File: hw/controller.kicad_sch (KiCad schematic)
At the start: 18 parts, among them J201 43650-0227, U201 NUCLEO-L432KC

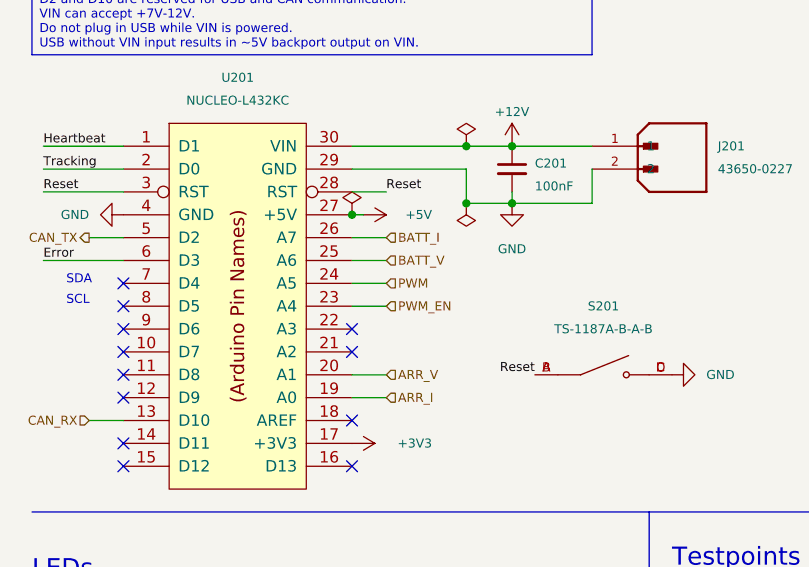
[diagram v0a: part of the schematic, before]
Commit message: bugfix for wrong adc pin for batt current measurements
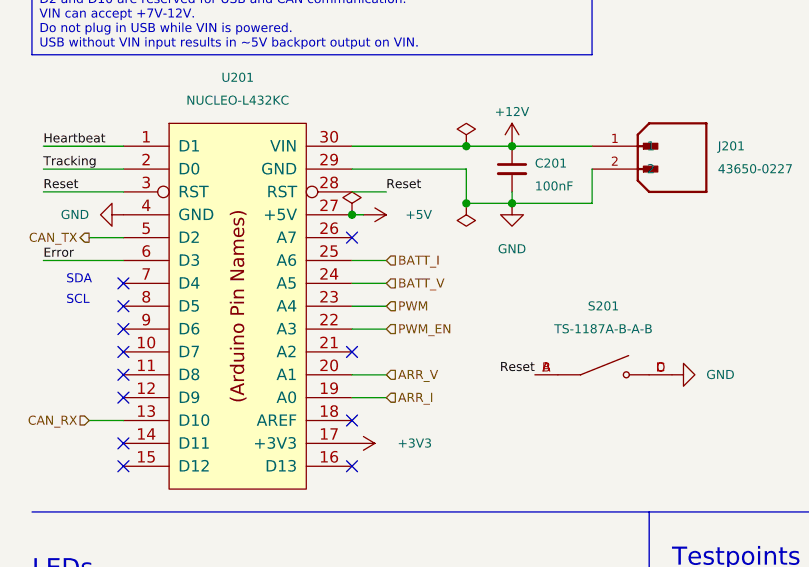
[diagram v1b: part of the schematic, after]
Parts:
- C201: Cost 0.0068 -> 0.0063; LCSC Part # C307331 -> CL05B104KB54PNC; Notes (none) -> Rated for 50V.
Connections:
- net BATT_I: now also U201.25 (A6); no longer U201.26 (A7)
- net BATT_V: now also U201.24 (A5); no longer U201.25 (A6)
- net PWM: now also U201.23 (A4); no longer U201.24 (A5)
- net PWM_EN: now also U201.22 (A3); no longer U201.23 (A4)
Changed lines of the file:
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@@
   (no_connect (at 170.18 82.55))
   (no_connect (at 144.78 74.93))
-  (no_connect (at 170.18 72.39))
   (no_connect (at 144.78 80.01))
   (no_connect (at 144.78 67.31))
   (no_connect (at 170.18 87.63))
   (no_connect (at 144.78 77.47))
+  (no_connect (at 170.18 62.23))
   (no_connect (at 144.78 69.85))
   (no_connect (at 144.78 87.63))
@@
     (stroke (width 0) (type default))
   )
-  (wire (pts (xy 173.99 69.85) (xy 170.18 69.85))
+  (wire (pts (xy 170.18 69.85) (xy 173.99 69.85))
     (stroke (width 0) (type default))
   )
@@
     (stroke (width 0) (type default))
   )
-  (wire (pts (xy 170.18 67.31) (xy 173.99 67.31))
+  (wire (pts (xy 187.96 58.42) (xy 196.85 58.42))
     (stroke (width 0) (type default))
   )
-  (wire (pts (xy 187.96 58.42) (xy 196.85 58.42))
+  (wire (pts (xy 170.18 64.77) (xy 173.99 64.77))
     (stroke (width 0) (type default))
   )
@@
     (stroke (width 0) (type default))
   )
-  (wire (pts (xy 173.99 64.77) (xy 170.18 64.77))
+  (wire (pts (xy 173.99 67.31) (xy 170.18 67.31))
     (stroke (width 0) (type default))
   )
-  (wire (pts (xy 170.18 62.23) (xy 173.99 62.23))
+  (wire (pts (xy 173.99 72.39) (xy 170.18 72.39))
     (stroke (width 0) (type default))
   )
@@
     (effects (font (size 1 1)) (justify left))
   )
-  (hierarchical_label "BATT_I" (shape input) (at 173.99 62.23 0) (fields_autoplaced)
-    (effects (font (size 1 1)) (justify left))
-  )
   (hierarchical_label "CAN_RX" (shape input) (at 140.97 82.55 180) (fields_autoplaced)
     (effects (font (size 1 1)) (justify right))
   )
-  (hierarchical_label "CAN_RX" (shape input) (at 190.5 105.41 0) (fields_autoplaced)
+  (hierarchical_label "BATT_V" (shape input) (at 173.99 67.31 0) (fields_autoplaced)
     (effects (font (size 1 1)) (justify left))
   )
-  (hierarchical_label "CAN_TX" (shape input) (at 179.07 105.41 0) (fields_autoplaced)
+  (hierarchical_label "PWM" (shape input) (at 173.99 69.85 0) (fields_autoplaced)
     (effects (font (size 1 1)) (justify left))
   )
-  (hierarchical_label "BATT_V" (shape input) (at 173.99 64.77 0) (fields_autoplaced)
+  (hierarchical_label "BATT_I" (shape input) (at 173.99 64.77 0) (fields_autoplaced)
     (effects (font (size 1 1)) (justify left))
   )
-  (hierarchical_label "PWM" (shape input) (at 173.99 67.31 0) (fields_autoplaced)
+  (hierarchical_label "CAN_RX" (shape input) (at 190.5 105.41 0) (fields_autoplaced)
     (effects (font (size 1 1)) (justify left))
   )
-  (hierarchical_label "PWM_EN" (shape input) (at 173.99 69.85 0) (fields_autoplaced)
+  (hierarchical_label "CAN_TX" (shape input) (at 179.07 105.41 0) (fields_autoplaced)
+    (effects (font (size 1 1)) (justify left))
+  )
+  (hierarchical_label "PWM_EN" (shape input) (at 173.99 72.39 0) (fields_autoplaced)
     (effects (font (size 1 1)) (justify left))
   )
@@
       (effects (font (size 1 1)) hide)
     )
-    (property "Datasheet" "https://datasheet.lcsc.com/lcsc/1810191222_Samsung-Electro-Mechanics-CL05B104KB54PNC_C307331.pdf" (at 187.96 54.61 0)
+    (property "Datasheet" "https://datasheet.lcsc.com/lcsc/2304140030_Samsung-Electro-Mechanics-CL05B104KB54PNC_C307331.pdf" (at 187.96 54.61 0)
       (effects (font (size 1 1)) hide)
     )
@@
       (effects (font (size 1 1)) hide)
     )
-    (property "LCSC Part #" "C307331" (at 187.96 54.61 0)
+    (property "LCSC Part #" "CL05B104KB54PNC" (at 187.96 54.61 0)
       (effects (font (size 1 1)) hide)
     )
-    (property "Cost" "0.0068" (at 187.96 54.61 0)
+    (property "Cost" "0.0063" (at 187.96 54.61 0)
       (effects (font (size 1 1)) hide)
     )
+    (property "Notes" "Rated for 50V." (at 187.96 54.61 0)
+      (effects (font (size 1.27 1.27)) hide)
+    )
     (pin "1")

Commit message: init sch changes
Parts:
- added C1: 10uF, symbol Device:C_Small
- added C10: 1uF, symbol Device:C_Small
- added C2, C3, C4, C6, C7, C8, C9: 100nF, symbol Device:C_Small
- added C5: 4.7uF, symbol Device:C_Small
- added D10, D9: GREEN, symbol Device:LED_Small
- added D11, D12: BLUE, symbol Device:LED_Small
- added D8: YELLOW, symbol Device:LED_Small
- added FB1: FerriteBead, symbol Device:FerriteBead
- added R15, R16, R17, R18, R19: 330, symbol Device:R_Small
- added SW1: SW_DPST, symbol Switch:SW_DPST
- added U1: STM32F446RETx, Package_QFP:LQFP-64_10x10mm_P0.5mm, symbol MCU_ST_STM32F4:STM32F446RETx
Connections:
- net GND: now also C1.2, C10.2, C2.1, C3.2, C4.2, C5.2, C6.2, C7.2, C8.2, C9.2, SW1.1, SW1.3, U1.12 (VSSA), U1.18 (VSS), U1.31 (VSS), U1.47 (VSS), U1.63 (VSS)
- new net: D8.2 (A), R15.2
- new net: D11.2 (A), R18.2
- new net: C5.1, U1.30 (VCAP_1)
- new net: C2.2, SW1.2, SW1.4, U1.7 (NRST)
- new net: D12.2 (A), R19.2
- new net: D9.2 (A), R16.2
- new net: D10.2 (A), R17.2
- new net VDD: C1.1, C3.1, C4.1, C6.1, C7.1, C8.1, FB1.1, U1.1 (VBAT), U1.19 (VDD), U1.32 (VDD), U1.48 (VDD), U1.64 (VDD)
- new net VDDA: C10.1, C9.1, FB1.2, U1.13 (VDDA)
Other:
- note added: "<1Ω ESR"
- note added: "Per V_{DD}"
- note added: "Power Regulation"
- note added: "To hit 180 MHZ F_{IO}, need 10 pF C_{L}"
- note added: "V_{BAT}"
- moved on the sheet: D201, D202, D203, D204, D205, R201, R202, R203, R204, R205

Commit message: v0.3.0rc (v1.0.0rc) sch complete
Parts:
- removed D10, D9: GREEN, symbol Device:LED_Small
- removed D11, D12: BLUE, symbol Device:LED_Small
- removed D201: YELLOW, LED_SMD:LED_0603_1608Metric, symbol Device:LED
- removed D202, D203: GREEN, LED_SMD:LED_0603_1608Metric, symbol Device:LED
- removed D204, D205: BLUE, LED_SMD:LED_0603_1608Metric, symbol Device:LED
- removed J201: 43650-0227, footprints:molex_microfit_43650_0227, symbol molex_microfit_43650_0227:43650-0227
- removed R16, R17, R18, R19: 330, symbol Device:R_Small
- removed R201, R202, R203, R204, R205: 100, Resistor_SMD:R_0402_1005Metric, symbol Device:R
- removed S201: TS-1187A-B-A-B, footprints:xkb_TS_1187A_B_A_B, symbol xkb_TS_1187A_B_A_B:TS-1187A-B-A-B
- removed TP201: 3V3 TP, TestPoint:TestPoint_Pad_1.0x1.0mm, symbol Connector:TestPoint
- removed TP202: 5V TP, TestPoint:TestPoint_Pad_1.0x1.0mm, symbol Connector:TestPoint
- removed TP203: GND TP, TestPoint:TestPoint_Pad_1.0x1.0mm, symbol Connector:TestPoint
- removed TP204: 12V TP, TestPoint:TestPoint_Pad_1.0x1.0mm, symbol Connector:TestPoint
- removed U201: NUCLEO-L432KC, footprints:stm_nucleo_L432KC, symbol stm_nucleo_L432KC:NUCLEO-L432KC
- added C202, C206: 4.3p, Resistor_SMD:R_0402_1005Metric, symbol Device:C_Small
- added C205: 6p, Resistor_SMD:R_0402_1005Metric, symbol Device:C_Small
- added D201, D205, D207: GRN, LED_SMD:LED_0402_1005Metric, symbol Device:LED_Small
- added D202, D204, D206, D208, D209, D210, D211, D212, D213, D214: BLU, LED_SMD:LED_0402_1005Metric, symbol Device:LED_Small
- added J201: UART Header, footprints:molex_microfit_43650_0427, symbol Connector_Generic:Conn_01x04
- added J202: Conn_ARM_SWD_TagConnect_TC2030-NL, Connector:Tag-Connect_TC2030-IDC-NL_2x03_P1.27mm_Vertical, symbol Connector:Conn_ARM_SWD_TagConnect_TC2030-NL
- added J203: USB_C_Plug_USB2.0, Connector_USB:USB_C_Receptacle_GCT_USB4105-xx-A_16P_TopMnt_Horizontal, symbol Connector:USB_C_Receptacle_USB2.0_16P
- added JP201, JP202: Jumper_2_Bridged, Connector_PinHeader_2.54mm:PinHeader_1x02_P2.54mm_Vertical, symbol Jumper:Jumper_2_Bridged
- added R201, R202, R203, R204, R206, R207, R208, R209, R210, R211, R212, R215, R216, R217, R218: 330, Resistor_SMD:R_0402_1005Metric, symbol Device:R_Small
- added R213, R214: 5.1k, Resistor_SMD:R_0402_1005Metric, symbol Device:R_Small
- added R219: 10k, Resistor_SMD:R_0402_1005Metric, symbol Device:R_Small
- added R220: 47, Resistor_SMD:R_0402_1005Metric, symbol Device:R_Small
- added SB201: Jumper, Jumper:SolderJumper-2_P1.3mm_Open_TrianglePad1.0x1.5mm, symbol Jumper:SolderJumper_2_Bridged
- added U201: TVS, Package_TO_SOT_SMD:SOT-23-6, symbol Power_Protection:USBLC6-2SC6
- added Y201: 25MHz, Crystal:Crystal_SMD_Abracon_ABM8AIG-4Pin_3.2x2.5mm, symbol Device:Crystal_GND24
- added Y202: 32kHz, Crystal:Crystal_SMD_Abracon_ABS25-4Pin_8.0x3.8mm, symbol Device:Crystal_GND23
- C201: value 100nF -> 6p; footprint Capacitor_SMD:C_0402_1005Metric -> Resistor_SMD:R_0402_1005Metric; Cost 0.0063 -> 0.0044; Distributor JLCPCB -> LCSC; LCSC Part # CL05B104KB54PNC -> C318621; Manufacturer Samsung Electro-Mechanics -> Samsung Electromechanics; Notes Rated for 50V. -> (none); P/N CL05B104KB54PNC -> CL05C060CB5NNNC
- C203: renamed from C1; value 10uF -> 10u; footprint (none) -> Resistor_SMD:R_0805_2012Metric; Cost (none) -> 0.34; Distributor (none) -> Mouser; Manufacturer (none) -> Murata; P/N (none) -> GRT21BC71E106KE13L
- C204: renamed from C3; value 100nF -> 100n; footprint (none) -> Resistor_SMD:R_0402_1005Metric; Cost (none) -> 0.0046; Distributor (none) -> LCSC; LCSC Part # (none) -> C307331; Manufacturer (none) -> Samsung Electromechanics; P/N (none) -> CL05B104KB54PNC
- C207: renamed from C2; value 100nF -> 100n; footprint (none) -> Resistor_SMD:R_0402_1005Metric; Cost (none) -> 0.0046; Distributor (none) -> LCSC; LCSC Part # (none) -> C307331; Manufacturer (none) -> Samsung Electromechanics; P/N (none) -> CL05B104KB54PNC
- C208: renamed from C4; value 100nF -> 100n; footprint (none) -> Resistor_SMD:R_0402_1005Metric; Cost (none) -> 0.0046; Distributor (none) -> LCSC; LCSC Part # (none) -> C307331; Manufacturer (none) -> Samsung Electromechanics; P/N (none) -> CL05B104KB54PNC
- C209: renamed from C6; value 100nF -> 100n; footprint (none) -> Resistor_SMD:R_0402_1005Metric; Cost (none) -> 0.0046; Distributor (none) -> LCSC; LCSC Part # (none) -> C307331; Manufacturer (none) -> Samsung Electromechanics; P/N (none) -> CL05B104KB54PNC
- C210: renamed from C5; value 4.7uF -> 4.7u; footprint (none) -> Resistor_SMD:R_0402_1005Metric; Cost (none) -> 0.0149; Distributor (none) -> LCSC; LCSC Part # (none) -> C318563; Manufacturer (none) -> Samsung Electromechanics; Notes (none) -> Low ESR <1Ohm as specified in datasheet.; P/N (none) -> CL05A475MO5NUNC
- C211: renamed from C7; value 100nF -> 100n; footprint (none) -> Resistor_SMD:R_0402_1005Metric; Cost (none) -> 0.0046; Distributor (none) -> LCSC; LCSC Part # (none) -> C307331; Manufacturer (none) -> Samsung Electromechanics; P/N (none) -> CL05B104KB54PNC
- C212: renamed from C8; value 100nF -> 100n; footprint (none) -> Resistor_SMD:R_0402_1005Metric; Cost (none) -> 0.0046; Distributor (none) -> LCSC; LCSC Part # (none) -> C307331; Manufacturer (none) -> Samsung Electromechanics; P/N (none) -> CL05B104KB54PNC
- C213: renamed from C9; value 100nF -> 100n; footprint (none) -> Resistor_SMD:R_0402_1005Metric; Cost (none) -> 0.0046; Distributor (none) -> LCSC; LCSC Part # (none) -> C307331; Manufacturer (none) -> Samsung Electromechanics; P/N (none) -> CL05B104KB54PNC
- C214: renamed from C10; value 1uF -> 1u; footprint (none) -> Resistor_SMD:R_0402_1005Metric; Cost (none) -> 0.0068; Distributor (none) -> LCSC; LCSC Part # (none) -> C307454; Manufacturer (none) -> Samsung Electromechanics; P/N (none) -> CL05X105KA5NQNC
- D203: renamed from D8; value YELLOW -> RED; footprint (none) -> LED_SMD:LED_0402_1005Metric; Cost (none) -> 0.51; Distributor (none) -> Mouser; Manufacturer (none) -> Wurth Elektronik; Notes (none) -> Target V_FWD=1.7V, I_D=2mA; P/N (none) -> 150040SS73220
- FB201: renamed from FB1; footprint (none) -> Resistor_SMD:R_0402_1005Metric; Cost (none) -> 0.1; Distributor (none) -> Mouser; Manufacturer (none) -> Murata; P/N (none) -> BLM15AX601SZ1D
- R205: renamed from R15; value 330 -> 1k; footprint (none) -> Resistor_SMD:R_0402_1005Metric; Cost (none) -> 0.0005; Distributor (none) -> LCSC; LCSC Part # (none) -> C11702; Manufacturer (none) -> Uniroyal; P/N (none) -> 0402WGF1001TCE
- SW201: renamed from SW1; value SW_DPST -> SW_SPST; footprint (none) -> Button_Switch_SMD:SW_Push_1P1T_XKB_TS-1187A; symbol Switch:SW_DPST -> Switch:SW_SPST; Cost (none) -> 0.0164; Distributor (none) -> LCSC; LCSC Part # (none) -> C318884; Manufacturer (none) -> XKB Connection; P/N (none) -> TS-1187A-B-A-B
- U202: renamed from U1; Cost (none) -> 10.05; Distributor (none) -> Mouser; Manufacturer (none) -> STMicroelectronics; Notes (none) -> Selected based on sampling speed.; P/N (none) -> STM32F446RET6TR
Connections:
- net +12V is gone; now on net GND: C201.1
- net +3V3: now also SB201.2 (B)
- net CAN_RX: now also U202.33 (PB12), R206.1
- net CAN_TX: now also U202.34 (PB13), R204.1
- net Error: now also R205.1, U202.51 (PC10)
- net GND: now also D203.1 (K), C202.1, C205.1, C206.1, D201.1 (K), D202.1 (K), D204.1 (K), D205.1 (K), D206.1 (K), D207.1 (K), D208.1 (K), D209.1 (K), D210.1 (K), D211.1 (K), D212.1 (K), D213.1 (K), D214.1 (K), J201.4 (Pin_4), J202.5 (GND), J203.A1 (GND), J203.A12 (GND), J203.B1 (GND), J203.B12 (GND), J203.S1 (SHIELD), JP202.2 (B), R213.2, R214.2, U201.2 (GND), Y201.2, Y201.4; no longer C201.2, SW201.3
- net Heartbeat: now also U202.53 (PC12), R209.1
- net PWM: now also U202.21 (PA5), R218.1
- net Tracking: now also U202.52 (PC11), R207.1
- net VDD: now also J201.1 (Pin_1), J202.1 (VCC), JP201.2 (B), R203.1, SB201.1 (A)
- net TEMP_SWL: now reaches U202.10 (PC2)
- net TEMP_GATE: now reaches U202.11 (PC3)
- net V_{ARR}: now reaches U202.14 (PA0)
- net I_{ARR}: now reaches U202.15 (PA1)
- net EN_INP: now reaches U202.16 (PA2)
- net EN_INP: now also R211.1
- net EN_INP_LD: now reaches U202.17 (PA3)
- net EN_INP_LD: now also R215.1
- net EN_PWM: now reaches U202.20 (PA4)
- net EN_PWM: now also R217.1
- net EN_OUT_LD: now reaches U202.22 (PA6)
- net EN_OUT_LD: now also R216.1
- net EN_OUT: now reaches U202.23 (PA7)
- net EN_OUT: now also R212.1
- net V_{BAT}: now reaches U202.24 (PC4)
- net I_{BAT}: now reaches U202.25 (PC5)
- net LSE_IN: now reaches U202.3 (PC14)
- net LSE_IN: now also C202.2, Y202.1
- net LSE_OUT: now reaches U202.4 (PC15)
- net LSE_OUT: now also C206.2, Y202.4
- net UART1_TX: now reaches U202.42 (PA9)
- net UART1_TX: now also R201.2, R208.1
- net UART1_RX: now reaches U202.43 (PA10)
- net UART1_RX: now also R202.2, R210.1
- net USBDM: now reaches U202.44 (PA11)
- net USBDM: now also U201.6 (I/O1)
- net USBDP: now reaches U202.45 (PA12)
- net USBDP: now also U201.4 (I/O2)
- net SWDIO: now reaches U202.46 (PA13)
- net SWDIO: now also J202.2 (SWDIO)
- net SWCLK: now reaches U202.49 (PA14)
- net SWCLK: now also J202.4 (SWCLK)
- net HSE_IN: now reaches U202.5 (PH0)
- net HSE_IN: now also C201.2, Y201.1
- net SWO: now reaches U202.55 (PB3)
- net SWO: now also J202.6 (SWO)
- net HSE_OUT: now reaches U202.6 (PH1)
- net HSE_OUT: now also R220.1
- net BOOT0: now reaches U202.60 (BOOT0)
- net BOOT0: now also R219.1
- net ISO_EN: now reaches U202.61 (PB8)
- net PROT_EN: now reaches U202.62 (PB9)
- net NRST: now reaches C207.2, SW201.2 (B), U202.7 (NRST)
- net NRST: now also J202.3 (~{RESET}); no longer SW201.4
- net TEMP_IND: now reaches U202.8 (PC0)
- net TEMP_SWH: now reaches U202.9 (PC1)
- new net: JP201.1 (A), JP202.1 (A), R219.2
- new net: D211.2 (A), R215.2
- new net: J203.B5 (CC2), R213.1
- new net: D204.2 (A), R206.2
- new net: C205.2, R220.2, Y201.3
- new net: J201.3 (Pin_3), R202.1
- new net: J203.A7 (D-), J203.B7 (D-), U201.1 (I/O1)
- new net: J203.A6 (D+), J203.B6 (D+), U201.3 (I/O2)
- new net: D214.2 (A), R218.2
- new net: D202.2 (A), R204.2
- new net: J201.2 (Pin_2), R201.1
- new net: D207.2 (A), R209.2
- new net: D208.2 (A), R210.2
- new net: D210.2 (A), R212.2
- new net: D206.2 (A), R208.2
- new net: D213.2 (A), R217.2
- new net: D205.2 (A), R207.2
- new net: D201.2 (A), R203.2
- new net: D209.2 (A), R211.2
- new net: J203.A5 (CC1), R214.1
- new net: D212.2 (A), R216.2
- new net VBUS: J203.A4 (VBUS), J203.A9 (VBUS), J203.B4 (VBUS), J203.B9 (VBUS), U201.5 (VBUS)
- no-connect marks 12 -> 22
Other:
- note added: "1% TOL"
- note added: "4.5-5.5V (nom 5V, 1.5A) for 5.1k PD resistors"
- note added: "Arbitrary. Needs backing math to approve."
- note added: "Assume stray capacitance is 5pF; derive C_{L1|L2} from sec. 3.3 in STM AN2867."
- note added: "Microcontroller"
- note removed: "<1Ω ESR"
- note removed: "Controller"
- note removed: "LEDs"
- note removed: "Power Regulation"
- note removed: "SCL"
- note removed: "SDA"
- note removed: "Testpoints"
- moved on the sheet: C203, C204, C207, C208, C209, C210, C211, C212, C213, C214, D203, FB201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

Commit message: HW sch changes, further layout progression
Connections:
- net ~{LKO_CLR}: now reaches U202.38 (PC7)
- net ~{LKO_LDAC}: now reaches U202.39 (PC8)
- net LKO_SDA: now reaches U202.40 (PC9)
- net LKO_SCL: now reaches U202.41 (PA8)
- no-connect marks 22 -> 18
